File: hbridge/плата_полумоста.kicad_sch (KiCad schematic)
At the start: 0 parts

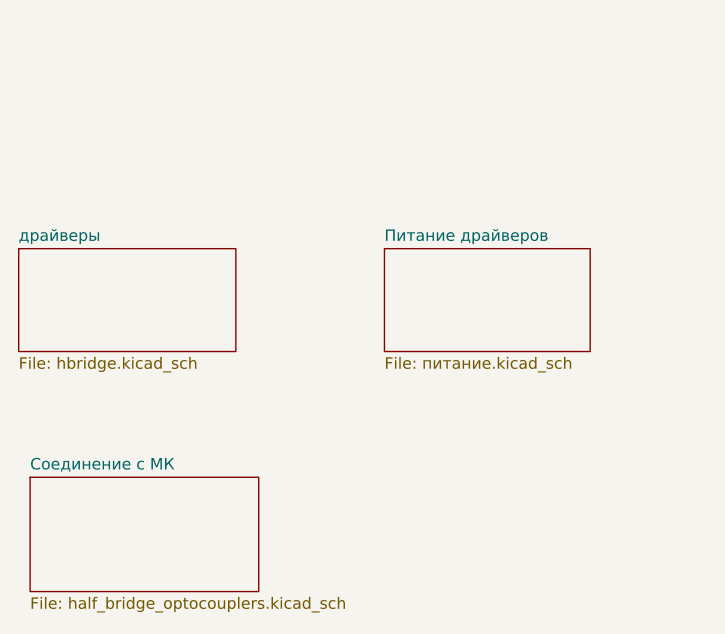
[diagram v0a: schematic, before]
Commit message: Half-bridge board: driver defence circuit added.
Logical circuit on AND, NOT, RS-latch, Shift-register.
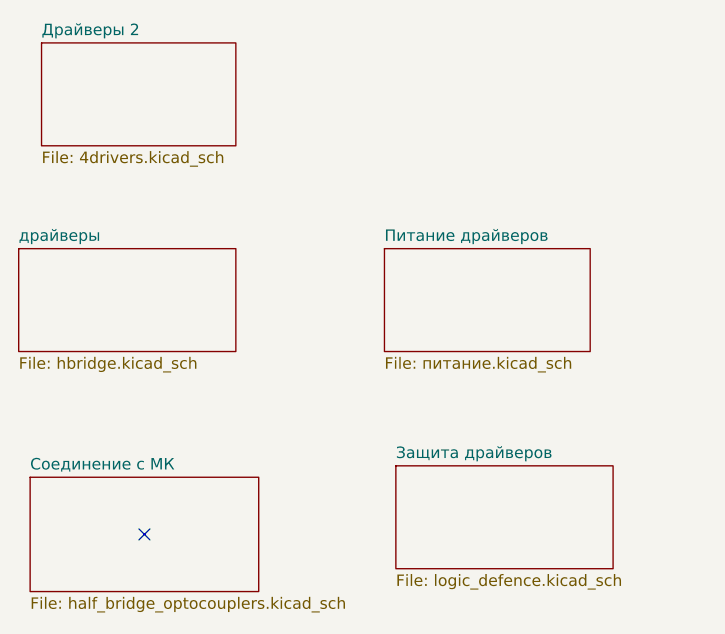
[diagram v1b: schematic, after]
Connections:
- no-connect marks 0 -> 1
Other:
- added sheet Драйверы 2 (4drivers.kicad_sch)
- added sheet Защита драйверов (logic_defence.kicad_sch)
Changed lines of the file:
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@@
 	(generator_version "10.0")
 	(paper "A4")
+	(no_connect
+		(at 74.93 92.71)
+	)
 	(sheet
 		(at 62.23 86.36)
@@
 				)
 			)
+		)
+	)
+	(sheet
+		(at 102.87 85.09)
+		(size 24.13 11.43)
+		(exclude_from_sim no)
+		(in_bom yes)
+		(on_board yes)
+		(dnp no)
+		(fields_autoplaced yes)
+		(stroke
+			(width 0.1524)
+			(type solid)
+		)
+		(fill
+			(color 0 0 0 0)
+		)
+		(property "Sheetname" "Защита драйверов"
+			(at 102.87 84.3784 0)
+			(show_name no)
+			(do_not_autoplace no)
+			(effects
+				(font
+					(size 1.27 1.27)
+				)
+				(justify left bottom)
+			)
+		)
+		(property "Sheetfile" "logic_defence.kicad_sch"
+			(at 102.87 97.1046 0)
+			(show_name no)
+			(do_not_autoplace no)
+			(effects
+				(font
+					(size 1.27 1.27)
+				)
+				(justify left top)
+			)
+		)
+		(instances
+			(project "hbridge"
+				(path "/96bc687b-1f0f-4b2f-95bf-a0725acd0403"
+					(page "5")
+				)
+			)
+		)
+	)
+	(sheet
+		(at 63.5 38.1)
+		(size 21.59 11.43)
+		(exclude_from_sim no)
+		(in_bom yes)
+		(on_board yes)
+		(dnp no)
+		(fields_autoplaced yes)
+		(stroke
+			(width 0.1524)
+			(type solid)
+		)
+		(fill
+			(color 0 0 0 0)
+		)
+		(property "Sheetname" "Драйверы 2"
+			(at 63.5 37.3884 0)
+			(show_name no)
+			(do_not_autoplace no)
+			(effects
+				(font
+					(size 1.27 1.27)
+				)
+				(justify left bottom)
+			)
+		)
+		(property "Sheetfile" "4drivers.kicad_sch"
+			(at 63.5 50.1146 0)
+			(show_name no)
+			(do_not_autoplace no)
+			(effects
+				(font
+					(size 1.27 1.27)
+				)
+				(justify left top)
+			)
+		)
+		(property "Field2" ""
+			(at 63.5 38.1 0)
+			(hide yes)
+			(show_name no)
+			(do_not_autoplace no)
+			(effects
+				(font
+					(size 1.27 1.27)
+				)
+			)
+		)
+		(instances
+			(project "hbridge"
+				(path "/96bc687b-1f0f-4b2f-95bf-a0725acd0403"
+					(page "6")
+				)
+			)

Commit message: Half-bridge refactoring start.
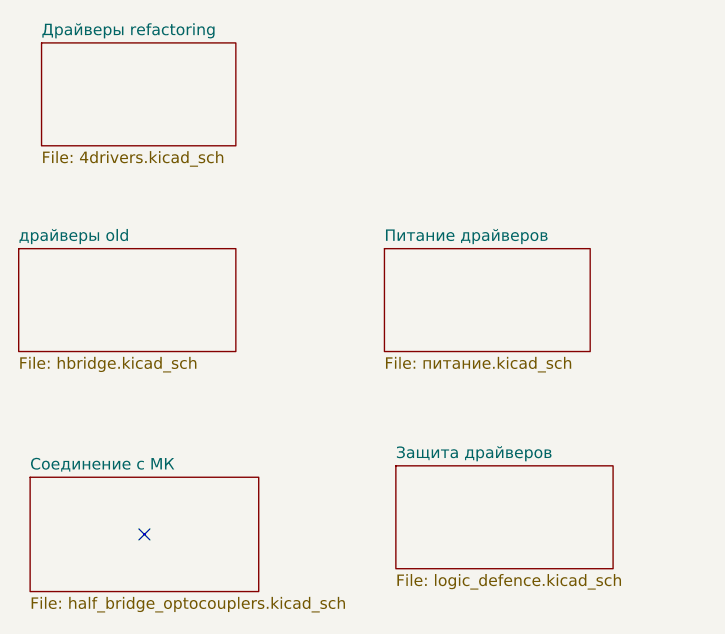
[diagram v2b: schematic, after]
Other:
- sheet Драйверы 2 renamed Драйверы refactoring
- sheet драйверы renamed драйверы old
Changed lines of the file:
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@@
 			(color 0 0 0 0)
 		)
-		(property "Sheetname" "Драйверы 2"
+		(property "Sheetname" "Драйверы refactoring"
 			(at 63.5 37.3884 0)
 			(show_name no)
@@
 			(project "hbridge"
 				(path "/96bc687b-1f0f-4b2f-95bf-a0725acd0403"
-					(page "6")
+					(page "2")
 				)
 			)
@@
 			(color 0 0 0 0)
 		)
-		(property "Sheetname" "драйверы"
+		(property "Sheetname" "драйверы old"
 			(at 60.96 60.2484 0)
 			(show_name no)
@@
 			(project "hbridge"
 				(path "/96bc687b-1f0f-4b2f-95bf-a0725acd0403"
-					(page "2")
+					(page "6")
 				)
 			)
